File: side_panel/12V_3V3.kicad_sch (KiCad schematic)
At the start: 10 parts, among them U10 TPS562201DDCR

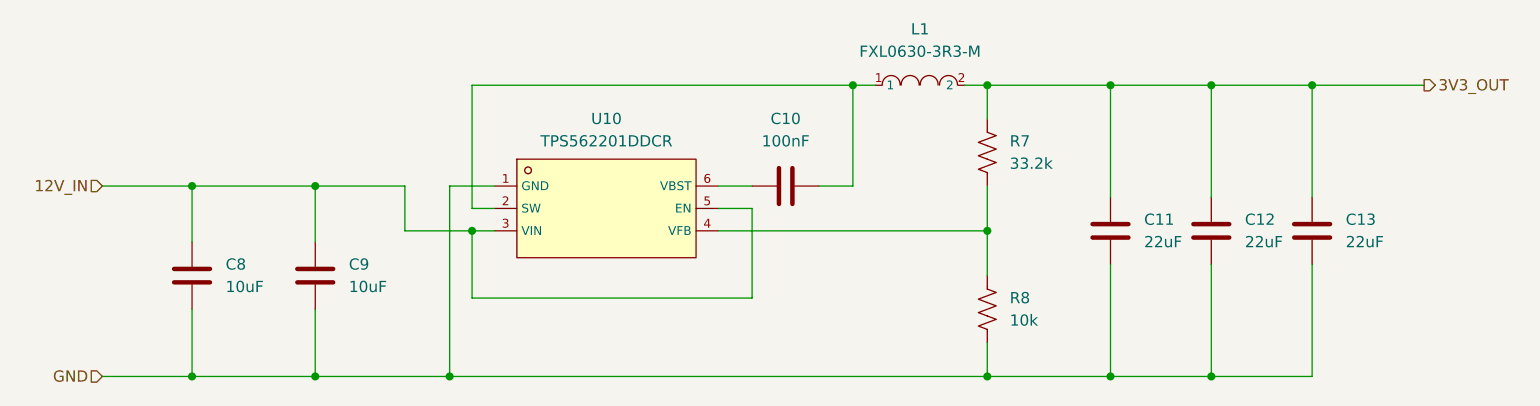
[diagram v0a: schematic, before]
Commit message: update: 拆分主控板和侧板至两个文件
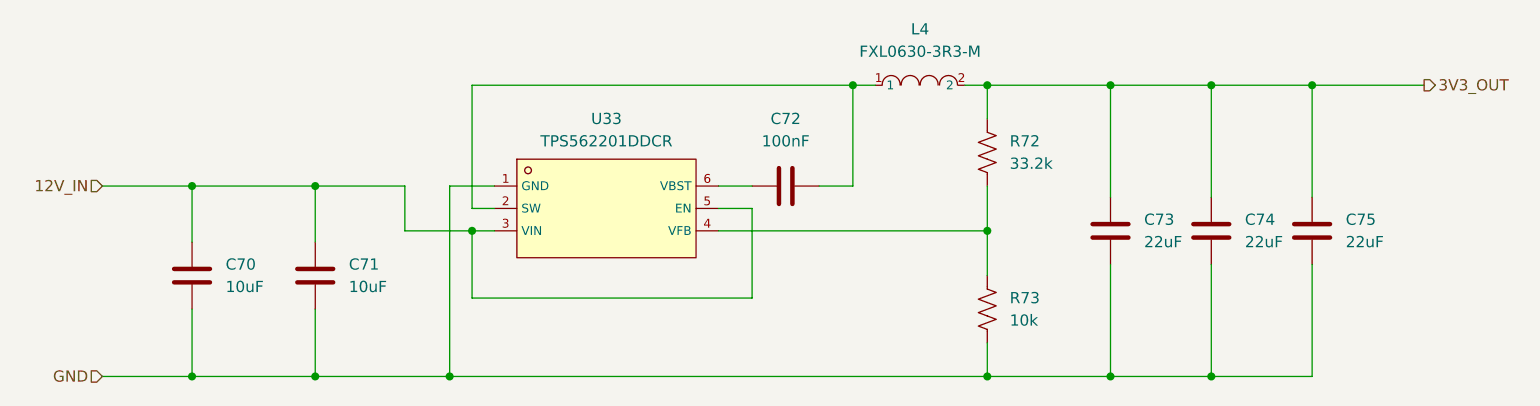
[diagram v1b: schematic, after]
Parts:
- renumbered C8 to C70, C9 to C71, C10 to C72, C11 to C73, C12 to C74, C13 to C75, L1 to L4, R7 to R72, R8 to R73, U10 to U33
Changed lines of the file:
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@@
 		(dnp no)
 		(fields_autoplaced yes)
-		(property "Reference" "C8"
+		(property "Reference" "C70"
 			(at 77.47 99.0599 0)
 			(show_name no)
@@
 		)
 		(instances
-			(project "overbed_table"
-				(path "/ea72387d-aa38-4027-b8fe-1f6fcfee6654/58200068-4715-4e07-a2e5-d4af79047f28"
-					(reference "C8")
+			(project "side_panel"
+				(path "/6f325c3b-cf1b-4cbd-9ec7-aa44385f0008/f010a35a-4b6a-457a-8fe3-87f1b650848c"
+					(reference "C70")
 					(unit 1)
 				)
@@
 		(dnp no)
 		(fields_autoplaced yes)
-		(property "Reference" "C9"
+		(property "Reference" "C71"
 			(at 91.44 99.0599 0)
 			(show_name no)
@@
 		)
 		(instances
-			(project "overbed_table"
-				(path "/ea72387d-aa38-4027-b8fe-1f6fcfee6654/58200068-4715-4e07-a2e5-d4af79047f28"
-					(reference "C9")
+			(project "side_panel"
+				(path "/6f325c3b-cf1b-4cbd-9ec7-aa44385f0008/f010a35a-4b6a-457a-8fe3-87f1b650848c"
+					(reference "C71")
 					(unit 1)
 				)
@@
 		(dnp no)
 		(fields_autoplaced yes)
-		(property "Reference" "R8"
+		(property "Reference" "R73"
 			(at 166.37 102.8699 90)
 			(show_name no)
@@
 		)
 		(instances
-			(project "overbed_table"
-				(path "/ea72387d-aa38-4027-b8fe-1f6fcfee6654/58200068-4715-4e07-a2e5-d4af79047f28"
-					(reference "R8")
+			(project "side_panel"
+				(path "/6f325c3b-cf1b-4cbd-9ec7-aa44385f0008/f010a35a-4b6a-457a-8fe3-87f1b650848c"
+					(reference "R73")
 					(unit 1)
 				)
@@
 		(dnp no)
 		(fields_autoplaced yes)
-		(property "Reference" "R7"
+		(property "Reference" "R72"
 			(at 166.37 85.0899 90)
 			(show_name no)
@@
 		)
 		(instances
-			(project "overbed_table"
-				(path "/ea72387d-aa38-4027-b8fe-1f6fcfee6654/58200068-4715-4e07-a2e5-d4af79047f28"
-					(reference "R7")
+			(project "side_panel"
+				(path "/6f325c3b-cf1b-4cbd-9ec7-aa44385f0008/f010a35a-4b6a-457a-8fe3-87f1b650848c"
+					(reference "R72")
 					(unit 1)
 				)
@@
 		(dnp no)
 		(fields_autoplaced yes)
-		(property "Reference" "U10"
+		(property "Reference" "U33"
 			(at 120.65 82.55 0)
 			(show_name no)
@@
 		)
 		(instances
-			(project "overbed_table"
-				(path "/ea72387d-aa38-4027-b8fe-1f6fcfee6654/58200068-4715-4e07-a2e5-d4af79047f28"
-					(reference "U10")
+			(project "side_panel"
+				(path "/6f325c3b-cf1b-4cbd-9ec7-aa44385f0008/f010a35a-4b6a-457a-8fe3-87f1b650848c"
+					(reference "U33")
 					(unit 1)
 				)
@@
 		(dnp no)
 		(fields_autoplaced yes)
-		(property "Reference" "C12"
+		(property "Reference" "C74"
 			(at 193.04 93.9799 0)
 			(show_name no)
@@
 		)
 		(instances
-			(project "overbed_table"
-				(path "/ea72387d-aa38-4027-b8fe-1f6fcfee6654/58200068-4715-4e07-a2e5-d4af79047f28"
-					(reference "C12")
+			(project "side_panel"
+				(path "/6f325c3b-cf1b-4cbd-9ec7-aa44385f0008/f010a35a-4b6a-457a-8fe3-87f1b650848c"
+					(reference "C74")
 					(unit 1)
 				)
@@
 		(dnp no)
 		(fields_autoplaced yes)
-		(property "Reference" "L1"
+		(property "Reference" "L4"
 			(at 156.21 72.39 0)
 			(show_name no)
@@
 		)
 		(instances
-			(project "overbed_table"
-				(path "/ea72387d-aa38-4027-b8fe-1f6fcfee6654/58200068-4715-4e07-a2e5-d4af79047f28"
-					(reference "L1")
+			(project "side_panel"
+				(path "/6f325c3b-cf1b-4cbd-9ec7-aa44385f0008/f010a35a-4b6a-457a-8fe3-87f1b650848c"
+					(reference "L4")
 					(unit 1)
 				)
@@
 		(dnp no)
 		(fields_autoplaced yes)
-		(property "Reference" "C10"
+		(property "Reference" "C72"
 			(at 140.97 82.55 90)
 			(show_name no)
@@
 		)
 		(instances
-			(project "overbed_table"
-				(path "/ea72387d-aa38-4027-b8fe-1f6fcfee6654/58200068-4715-4e07-a2e5-d4af79047f28"
-					(reference "C10")
+			(project "side_panel"
+				(path "/6f325c3b-cf1b-4cbd-9ec7-aa44385f0008/f010a35a-4b6a-457a-8fe3-87f1b650848c"
+					(reference "C72")
 					(unit 1)
 				)
@@
 		(dnp no)
 		(fields_autoplaced yes)
-		(property "Reference" "C11"
+		(property "Reference" "C73"
 			(at 181.61 93.9799 0)
 			(show_name no)
@@
 		)
 		(instances
-			(project "overbed_table"
-				(path "/ea72387d-aa38-4027-b8fe-1f6fcfee6654/58200068-4715-4e07-a2e5-d4af79047f28"
-					(reference "C11")
+			(project "side_panel"
+				(path "/6f325c3b-cf1b-4cbd-9ec7-aa44385f0008/f010a35a-4b6a-457a-8fe3-87f1b650848c"
+					(reference "C73")
 					(unit 1)
 				)
@@
 		(dnp no)
 		(fields_autoplaced yes)
-		(property "Reference" "C13"
+		(property "Reference" "C75"
 			(at 204.47 93.9799 0)
 			(show_name no)
@@
 		)
 		(instances
-			(project "overbed_table"
-				(path "/ea72387d-aa38-4027-b8fe-1f6fcfee6654/58200068-4715-4e07-a2e5-d4af79047f28"
-					(reference "C13")
+			(project "side_panel"
+				(path "/6f325c3b-cf1b-4cbd-9ec7-aa44385f0008/f010a35a-4b6a-457a-8fe3-87f1b650848c"
+					(reference "C75")
 					(unit 1)
 				)

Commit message: 更新针脚变动
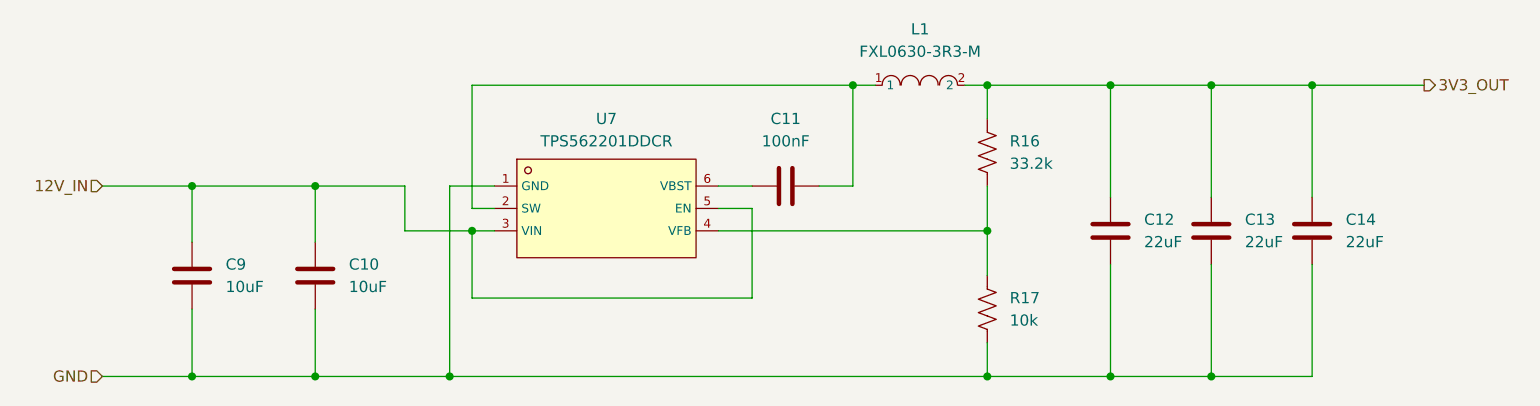
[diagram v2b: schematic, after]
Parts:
- R16: renamed from R72; footprint PCM_SparkFun-Resistor:R_0603_1608Metric -> Resistor_SMD:R_0603_1608Metric
- R17: renamed from R73; footprint PCM_SparkFun-Resistor:R_0603_1608Metric -> Resistor_SMD:R_0603_1608Metric
- renumbered C71 to C10, C72 to C11, C73 to C12, C74 to C13, C75 to C14, C70 to C9, L4 to L1, U33 to U7
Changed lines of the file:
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@@
 		(dnp no)
 		(fields_autoplaced yes)
-		(property "Reference" "C70"
+		(property "Reference" "C9"
 			(at 77.47 99.0599 0)
 			(show_name no)
@@
 			(project "side_panel"
 				(path "/6f325c3b-cf1b-4cbd-9ec7-aa44385f0008/f010a35a-4b6a-457a-8fe3-87f1b650848c"
-					(reference "C70")
+					(reference "C9")
 					(unit 1)
 				)
@@
 		(dnp no)
 		(fields_autoplaced yes)
-		(property "Reference" "C71"
+		(property "Reference" "C10"
 			(at 91.44 99.0599 0)
 			(show_name no)
@@
 			(project "side_panel"
 				(path "/6f325c3b-cf1b-4cbd-9ec7-aa44385f0008/f010a35a-4b6a-457a-8fe3-87f1b650848c"
-					(reference "C71")
+					(reference "C10")
 					(unit 1)
 				)
@@
 		(dnp no)
 		(fields_autoplaced yes)
-		(property "Reference" "R73"
+		(property "Reference" "R17"
 			(at 166.37 102.8699 90)
 			(show_name no)
@@
 			)
 		)
-		(property "Footprint" "PCM_SparkFun-Resistor:R_0603_1608Metric"
+		(property "Footprint" "Resistor_SMD:R_0603_1608Metric"
 			(at 159.258 104.14 0)
 			(hide yes)
@@
 			(project "side_panel"
 				(path "/6f325c3b-cf1b-4cbd-9ec7-aa44385f0008/f010a35a-4b6a-457a-8fe3-87f1b650848c"
-					(reference "R73")
+					(reference "R17")
 					(unit 1)
 				)
@@
 		(dnp no)
 		(fields_autoplaced yes)
-		(property "Reference" "R72"
+		(property "Reference" "R16"
 			(at 166.37 85.0899 90)
 			(show_name no)
@@
 			)
 		)
-		(property "Footprint" "PCM_SparkFun-Resistor:R_0603_1608Metric"
+		(property "Footprint" "Resistor_SMD:R_0603_1608Metric"
 			(at 159.258 86.36 0)
 			(hide yes)
@@
 			(project "side_panel"
 				(path "/6f325c3b-cf1b-4cbd-9ec7-aa44385f0008/f010a35a-4b6a-457a-8fe3-87f1b650848c"
-					(reference "R72")
+					(reference "R16")
 					(unit 1)
 				)
@@
 		(dnp no)
 		(fields_autoplaced yes)
-		(property "Reference" "U33"
+		(property "Reference" "U7"
 			(at 120.65 82.55 0)
 			(show_name no)
@@
 			(project "side_panel"
 				(path "/6f325c3b-cf1b-4cbd-9ec7-aa44385f0008/f010a35a-4b6a-457a-8fe3-87f1b650848c"
-					(reference "U33")
+					(reference "U7")
 					(unit 1)
 				)
@@
 		(dnp no)
 		(fields_autoplaced yes)
-		(property "Reference" "C74"
+		(property "Reference" "C13"
 			(at 193.04 93.9799 0)
 			(show_name no)
@@
 			(project "side_panel"
 				(path "/6f325c3b-cf1b-4cbd-9ec7-aa44385f0008/f010a35a-4b6a-457a-8fe3-87f1b650848c"
-					(reference "C74")
+					(reference "C13")
 					(unit 1)
 				)
@@
 		(dnp no)
 		(fields_autoplaced yes)
-		(property "Reference" "L4"
+		(property "Reference" "L1"
 			(at 156.21 72.39 0)
 			(show_name no)
@@
 			(project "side_panel"
 				(path "/6f325c3b-cf1b-4cbd-9ec7-aa44385f0008/f010a35a-4b6a-457a-8fe3-87f1b650848c"
-					(reference "L4")
+					(reference "L1")
 					(unit 1)
 				)
@@
 		(dnp no)
 		(fields_autoplaced yes)
-		(property "Reference" "C72"
+		(property "Reference" "C11"
 			(at 140.97 82.55 90)
 			(show_name no)
@@
 			(project "side_panel"
 				(path "/6f325c3b-cf1b-4cbd-9ec7-aa44385f0008/f010a35a-4b6a-457a-8fe3-87f1b650848c"
-					(reference "C72")
+					(reference "C11")
 					(unit 1)
 				)
@@
 		(dnp no)
 		(fields_autoplaced yes)
-		(property "Reference" "C73"
+		(property "Reference" "C12"
 			(at 181.61 93.9799 0)
 			(show_name no)
@@
 			(project "side_panel"
 				(path "/6f325c3b-cf1b-4cbd-9ec7-aa44385f0008/f010a35a-4b6a-457a-8fe3-87f1b650848c"
-					(reference "C73")
+					(reference "C12")
 					(unit 1)
 				)
@@
 		(dnp no)
 		(fields_autoplaced yes)
-		(property "Reference" "C75"
+		(property "Reference" "C14"
 			(at 204.47 93.9799 0)
 			(show_name no)
@@
 			(project "side_panel"
 				(path "/6f325c3b-cf1b-4cbd-9ec7-aa44385f0008/f010a35a-4b6a-457a-8fe3-87f1b650848c"
-					(reference "C75")
+					(reference "C14")
 					(unit 1)
 				)
